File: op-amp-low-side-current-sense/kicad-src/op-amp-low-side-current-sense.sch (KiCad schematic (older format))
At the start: 10 parts, among them J2 Conn_01x04, Q1 2N3904BU, U1 AD8551RM

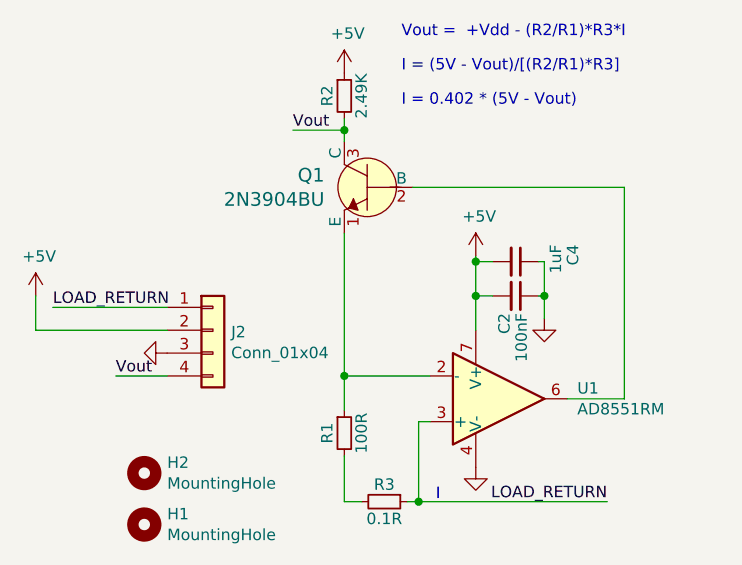
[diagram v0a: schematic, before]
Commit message: fix silkscreen error
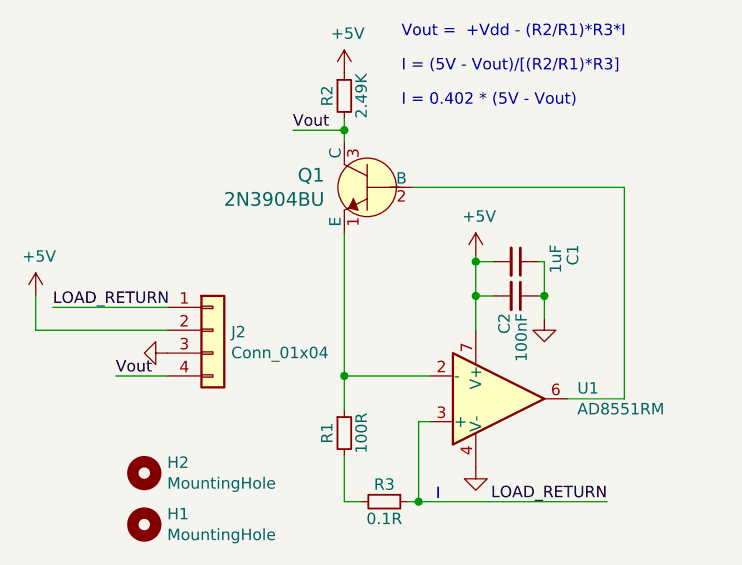
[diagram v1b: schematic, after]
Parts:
- renumbered C4 to C1
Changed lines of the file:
@@
 $EndComp
 $Comp
-L Device:C_Small C4
+L Device:C_Small C1
 U 1 1 61C7449E
 P 6150 3350
-F 0 "C4" H 6075 3600 50  0000 L CNN
+F 0 "C1" H 6075 3600 50  0000 L CNN
 F 1 "1uF" H 6075 3525 50  0000 L CNN
 F 2 "Capacitor_SMD:C_0603_1608Metric" H 6150 3350 50  0001 C CNN
